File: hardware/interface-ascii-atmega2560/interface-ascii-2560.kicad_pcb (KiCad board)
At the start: 2 copper layers, 88.9 x 132.1 mm, 50 parts, among them J1 Apple 2, J10 Keyboard, J2 Apple 1, J3 UART, J4 Conn_01x05, J5 SOL-20, J6 Program, J7 Custom Connector 1 / Proto, J8 Conn_01x25, SW1 Options, U1 ATmega2560-16AU, Y1 16.000 MHz

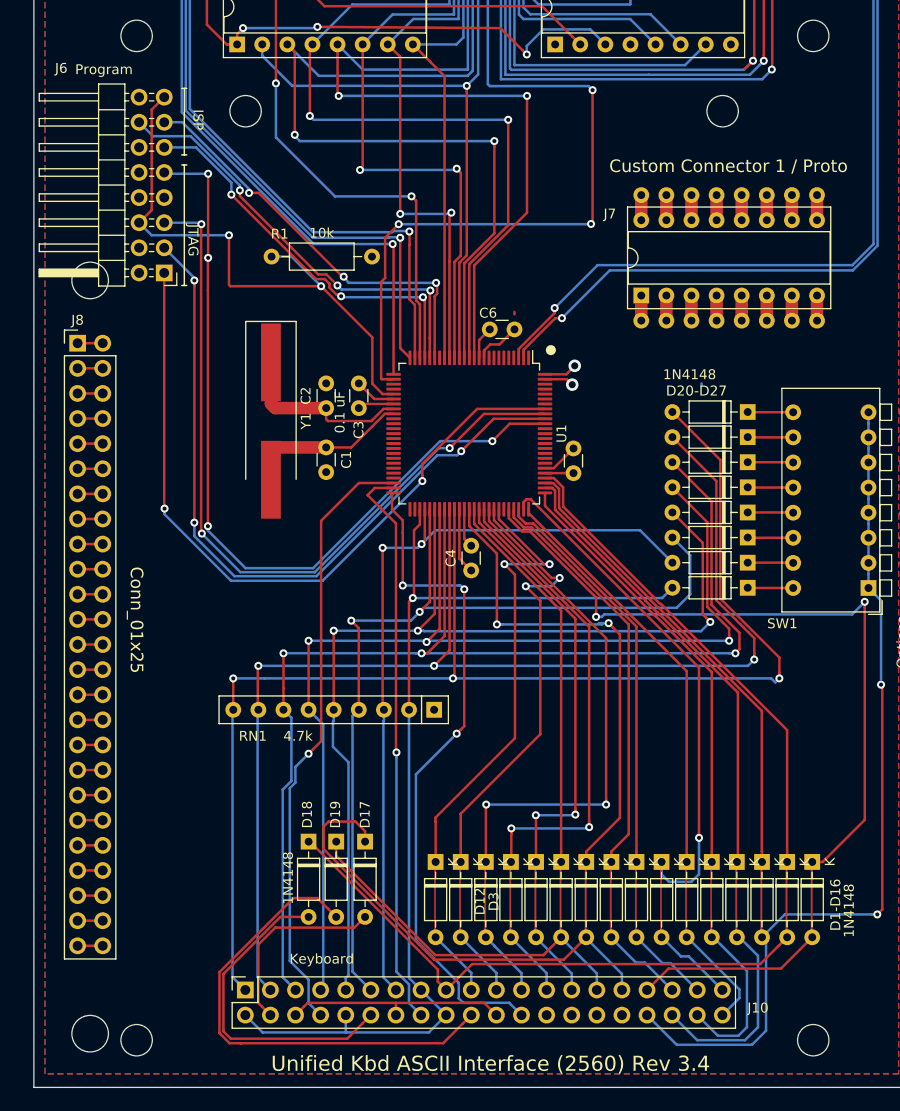
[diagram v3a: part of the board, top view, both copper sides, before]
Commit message: Various PCB cleanup
- Fix position of holes around 1x25 connector to match Apple 2 keyboard
- silk screen fixes
- minor trace shoves.
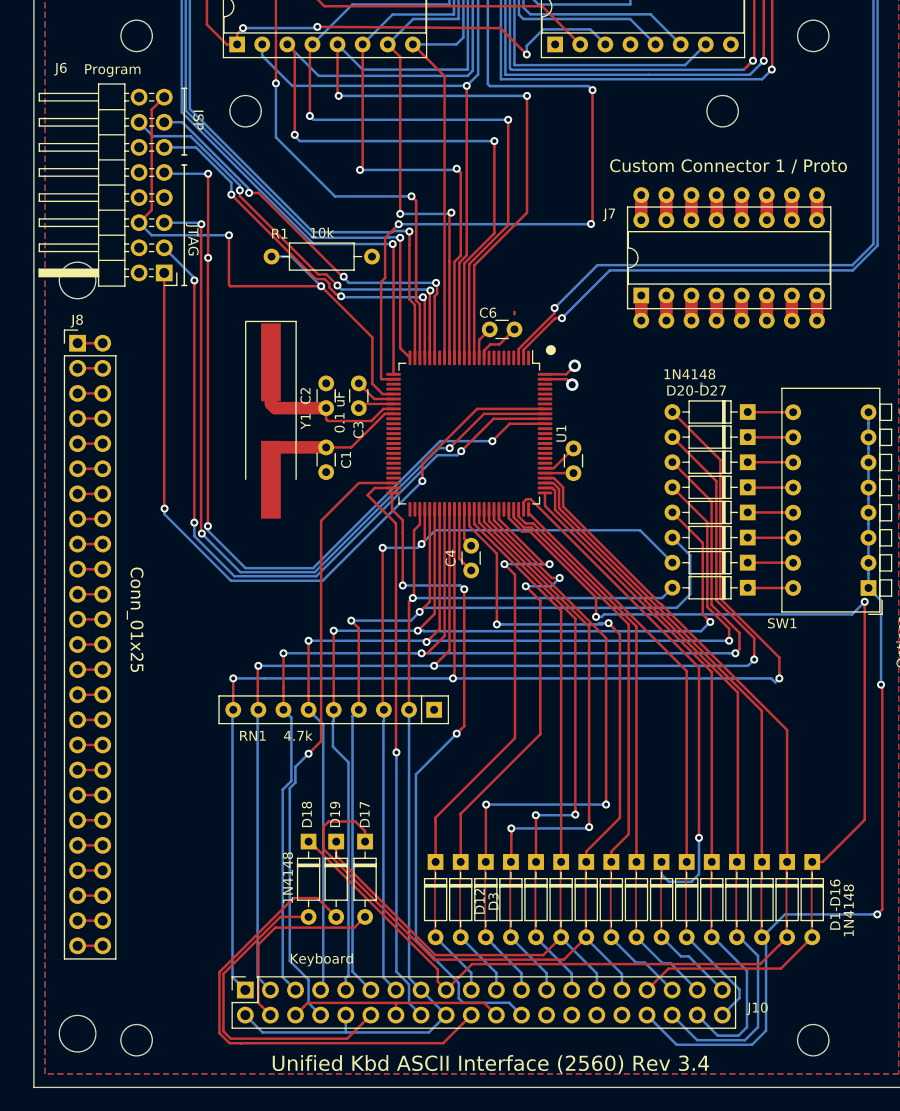
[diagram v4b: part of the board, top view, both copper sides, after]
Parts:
- moved MH1 1.27 mm to (168.3, 101.2)
- moved MH2 1.27 mm to (168.3, 177.4)
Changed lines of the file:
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@@
   (title_block
     (title "Unified Retro Keyboard ASCII Interface (2560)")
-    (date 2020-05-31)
+    (date 2020-06-02)
     (rev 3.4)
   )
@@
   )
   (module MountingHole:MountingHole_3.7mm (layer F.Cu)
-    (at 169.522 177.446)
+    (at 168.252 177.446)
     (descr "Mounting Hole 3.7mm, no annular")
     (tags "mounting hole 3.7mm no annular")
@@
   )
   (module MountingHole:MountingHole_3.7mm (layer F.Cu)
-    (at 169.522 101.246)
+    (at 168.252 101.246)
     (descr "Mounting Hole 3.7mm, no annular")
     (tags "mounting hole 3.7mm no annular")
@@
       (effects (font (size 1 1) (thickness 0.15)))
     )
+    (fp_circle (center 0 0) (end 3.7 0) (layer Cmts.User) (width 0.15))
     (fp_text user %R (at 0.3 0) (layer F.Fab) hide
       (effects (font (size 1 1) (thickness 0.15)))
     )
-    (fp_circle (center 0 0) (end 3.7 0) (layer Cmts.User) (width 0.15))
     (pad 1 np_thru_hole circle (at 0 0) (size 3.7 3.7) (drill 3.7) (layers *.Cu *.Mask))
   )
@@
       (effects (font (size 1 1) (thickness 0.15)))
     )
-    (fp_text value Program (at 6.096 20.574) (layer F.SilkS)
+    (fp_text value Program (at 5.207 20.574) (layer F.SilkS)
       (effects (font (size 1 1) (thickness 0.15)))
     )
@@
       (effects (font (size 0.8 0.8) (thickness 0.12)))
     )
-    (fp_text user K (at 0 -1.8 90) (layer F.SilkS)
-      (effects (font (size 1 1) (thickness 0.15)))
-    )
-    (fp_text user K (at 0 -1.8 90) (layer F.SilkS)
-      (effects (font (size 1 1) (thickness 0.15)))
-    )
     (pad 1 thru_hole rect (at 0 0 270) (size 1.6 1.6) (drill 0.8) (layers *.Cu *.Mask)
       (net 41 "Net-(D15-Pad1)"))
@@
       (effects (font (size 0.8 0.8) (thickness 0.12)))
     )
-    (fp_text user K (at 0 -1.8 90) (layer F.SilkS)
-      (effects (font (size 1 1) (thickness 0.15)))
-    )
-    (fp_text user K (at 0 -1.8 90) (layer F.SilkS)
-      (effects (font (size 1 1) (thickness 0.15)))
-    )
     (pad 1 thru_hole rect (at 0 0 270) (size 1.6 1.6) (drill 0.8) (layers *.Cu *.Mask)
       (net 49 "Net-(D6-Pad1)"))
@@
       (effects (font (size 0.8 0.8) (thickness 0.12)))
     )
-    (fp_text user K (at 0 -1.8 90) (layer F.SilkS)
-      (effects (font (size 1 1) (thickness 0.15)))
-    )
-    (fp_text user K (at 0 -1.8 90) (layer F.SilkS)
-      (effects (font (size 1 1) (thickness 0.15)))
-    )
     (pad 1 thru_hole rect (at 0 0 270) (size 1.6 1.6) (drill 0.8) (layers *.Cu *.Mask)
       (net 40 "Net-(D14-Pad1)"))
@@
       (effects (font (size 0.8 0.8) (thickness 0.12)))
     )
-    (fp_text user K (at 0 -1.8 90) (layer F.SilkS)
-      (effects (font (size 1 1) (thickness 0.15)))
-    )
-    (fp_text user K (at 0 -1.8 90) (layer F.SilkS)
-      (effects (font (size 1 1) (thickness 0.15)))
-    )
     (pad 1 thru_hole rect (at 0 0 270) (size 1.6 1.6) (drill 0.8) (layers *.Cu *.Mask)
       (net 48 "Net-(D5-Pad1)"))
@@
       (effects (font (size 0.8 0.8) (thickness 0.12)))
     )
-    (fp_text user K (at 0 -1.8 90) (layer F.SilkS)
-      (effects (font (size 1 1) (thickness 0.15)))
-    )
-    (fp_text user K (at 0 -1.8 90) (layer F.SilkS)
-      (effects (font (size 1 1) (thickness 0.15)))
-    )
     (pad 1 thru_hole rect (at 0 0 270) (size 1.6 1.6) (drill 0.8) (layers *.Cu *.Mask)
       (net 39 "Net-(D13-Pad1)"))
@@
       (effects (font (size 0.8 0.8) (thickness 0.12)))
     )
-    (fp_text user K (at 0 -1.8 90) (layer F.SilkS)
-      (effects (font (size 1 1) (thickness 0.15)))
-    )
-    (fp_text user K (at 0 -1.8 90) (layer F.SilkS)
-      (effects (font (size 1 1) (thickness 0.15)))
-    )
     (pad 1 thru_hole rect (at 0 0 270) (size 1.6 1.6) (drill 0.8) (layers *.Cu *.Mask)
       (net 51 "Net-(D8-Pad1)"))
@@
       (effects (font (size 0.8 0.8) (thickness 0.12)))
     )
-    (fp_text user K (at 0 -1.8 90) (layer F.SilkS)
-      (effects (font (size 1 1) (thickness 0.15)))
-    )
-    (fp_text user K (at 0 -1.8 90) (layer F.SilkS)
-      (effects (font (size 1 1) (thickness 0.15)))
-    )
     (pad 1 thru_hole rect (at 0 0 270) (size 1.6 1.6) (drill 0.8) (layers *.Cu *.Mask)
       (net 50 "Net-(D7-Pad1)"))
@@
       (effects (font (size 0.8 0.8) (thickness 0.12)))
     )
-    (fp_text user K (at 0 -1.8 90) (layer F.SilkS)
-      (effects (font (size 1 1) (thickness 0.15)))
-    )
-    (fp_text user K (at 0 -1.8 90) (layer F.SilkS)
-      (effects (font (size 1 1) (thickness 0.15)))
-    )
     (pad 1 thru_hole rect (at 0 0 270) (size 1.6 1.6) (drill 0.8) (layers *.Cu *.Mask)
       (net 42 "Net-(D16-Pad1)"))
@@
       (effects (font (size 0.8 0.8) (thickness 0.12)))
     )
-    (fp_text user K (at 0 -1.8 90) (layer F.SilkS) hide
-      (effects (font (size 1 1) (thickness 0.15)))
-    )
-    (fp_text user K (at 0 -1.8 90) (layer F.SilkS)
-      (effects (font (size 1 1) (thickness 0.15)))
-    )
     (pad 1 thru_hole rect (at 0 0 270) (size 1.6 1.6) (drill 0.8) (layers *.Cu *.Mask)
       (net 47 "Net-(D4-Pad1)"))
@@
       (effects (font (size 0.8 0.8) (thickness 0.12)))
     )
-    (fp_text user K (at 0 -1.8 90) (layer F.SilkS) hide
-      (effects (font (size 1 1) (thickness 0.15)))
-    )
-    (fp_text user K (at 0 -1.8 90) (layer F.SilkS)
-      (effects (font (size 1 1) (thickness 0.15)))
-    )
     (pad 1 thru_hole rect (at 0 0 270) (size 1.6 1.6) (drill 0.8) (layers *.Cu *.Mask)
       (net 38 "Net-(D12-Pad1)"))
@@
       (effects (font (size 0.8 0.8) (thickness 0.12)))
     )
-    (fp_text user K (at 0 -1.8 90) (layer F.SilkS) hide
-      (effects (font (size 1 1) (thickness 0.15)))
-    )
-    (fp_text user K (at 0 -1.8 90) (layer F.SilkS)
-      (effects (font (size 1 1) (thickness 0.15)))
-    )
     (pad 1 thru_hole rect (at 0 0 270) (size 1.6 1.6) (drill 0.8) (layers *.Cu *.Mask)
       (net 37 "Net-(D11-Pad1)"))
@@
       (effects (font (size 0.8 0.8) (thickness 0.12)))
     )
-    (fp_text user K (at 0 -1.8 90) (layer F.SilkS) hide
-      (effects (font (size 1 1) (thickness 0.15)))
-    )
-    (fp_text user K (at 0 -1.8 90) (layer F.SilkS)
-      (effects (font (size 1 1) (thickness 0.15)))
-    )
     (pad 1 thru_hole rect (at 0 0 270) (size 1.6 1.6) (drill 0.8) (layers *.Cu *.Mask)
       (net 53 "Net-(D10-Pad1)"))
@@
       (effects (font (size 0.8 0.8) (thickness 0.12)))
     )
-    (fp_text user K (at 0 -1.8 90) (layer F.SilkS) hide
-      (effects (font (size 1 1) (thickness 0.15)))
-    )
-    (fp_text user K (at 0 -1.8 90) (layer F.SilkS)
-      (effects (font (size 1 1) (thickness 0.15)))
-    )
     (pad 1 thru_hole rect (at 0 0 270) (size 1.6 1.6) (drill 0.8) (layers *.Cu *.Mask)
       (net 52 "Net-(D9-Pad1)"))
@@
       (effects (font (size 1 1) (thickness 0.15)))
     )
-    (fp_text user K (at 0 -1.8 90) (layer F.SilkS)
-      (effects (font (size 1 1) (thickness 0.15)))
-    )
     (pad 1 thru_hole rect (at 0 0 270) (size 1.6 1.6) (drill 0.8) (layers *.Cu *.Mask)
       (net 139 "Net-(D3-Pad1)"))
@@
       (effects (font (size 0.8 0.8) (thickness 0.12)))
     )
-    (fp_text user K (at 0 -1.8 90) (layer F.SilkS) hide
-      (effects (font (size 1 1) (thickness 0.15)))
-    )
-    (fp_text user K (at 0 -1.8 90) (layer F.SilkS)
-      (effects (font (size 1 1) (thickness 0.15)))
-    )
     (pad 1 thru_hole rect (at 0 0 270) (size 1.6 1.6) (drill 0.8) (layers *.Cu *.Mask)
       (net 138 "Net-(D2-Pad1)"))
@@
       (effects (font (size 0.8 0.8) (thickness 0.12)))
     )
-    (fp_text user K (at 0 -1.8 90) (layer F.SilkS) hide
-      (effects (font (size 1 1) (thickness 0.15)))
-    )
-    (fp_text user K (at 0 -1.8 90) (layer F.SilkS)
-      (effects (font (size 1 1) (thickness 0.15)))
-    )
     (pad 1 thru_hole rect (at 0 0 270) (size 1.6 1.6) (drill 0.8) (layers *.Cu *.Mask)
       (net 137 "Net-(D1-Pad1)"))
@@
     (connect_pads (clearance 0.508))
     (min_thickness 0.254)
-    (fill (arc_segments 32) (thermal_gap 0.508) (thermal_bridge_width 0.508))
+    (fill yes (arc_segments 32) (thermal_gap 0.508) (thermal_bridge_width 0.508))
     (polygon
       (pts
@@
     (connect_pads (clearance 0.508))
     (min_thickness 0.254)
-    (fill (arc_segments 32) (thermal_gap 0.508) (thermal_bridge_width 0.508))
+    (fill yes (arc_segments 32) (thermal_gap 0.508) (thermal_bridge_width 0.508))
     (polygon
       (pts
